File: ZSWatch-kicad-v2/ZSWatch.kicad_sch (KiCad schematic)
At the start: 71 parts, among them IC1 ESDALC6V1W5, IC2 XC9265C181MR-G, IC3 TPS61023DRLT, IC4 MAX30101EFD+T, IC5 FAN5622SX, IC6 BMI270, IC7 LIS2MDLTR, J2 Charger and programming heade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, M1 Vibrator DC Motor, U1 MAX1811ESA+, U10 0_NORA-B106, U11 NTS0104GU12, U13 GC9A01A_CST816S, U2 DMC2400UV-7, U3 NCV300LSN36T1G, U4 BMP581, U5 BME688, U6 DRV2603RUNT, U7 XC9265A331MR-G

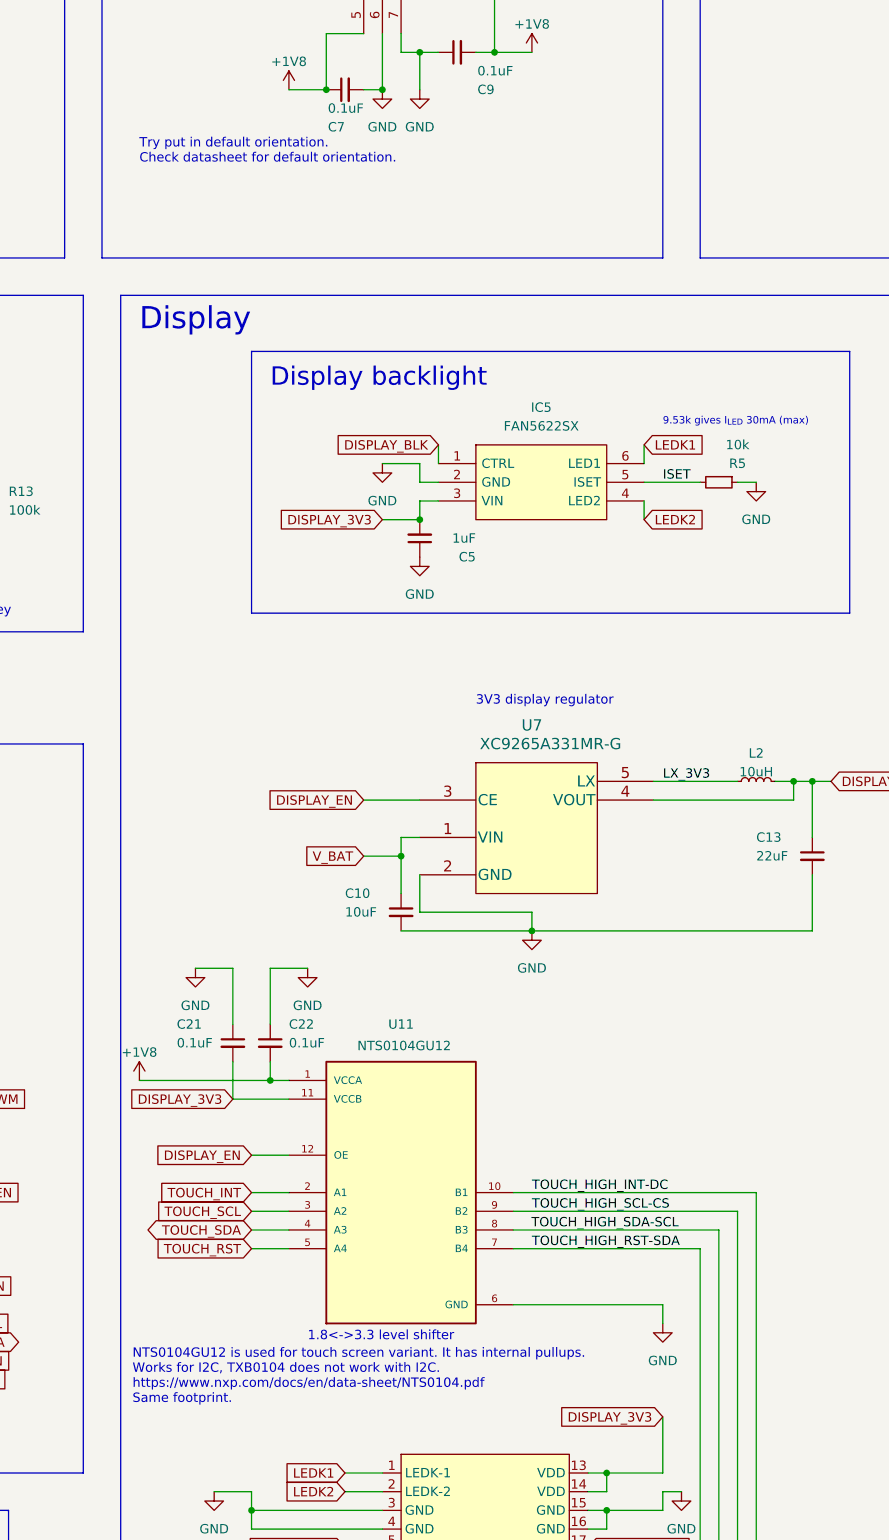
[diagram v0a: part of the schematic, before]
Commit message: Schematic: Re-generate latest schematic after some cleanup. Remove obsolete v1 kicad project.
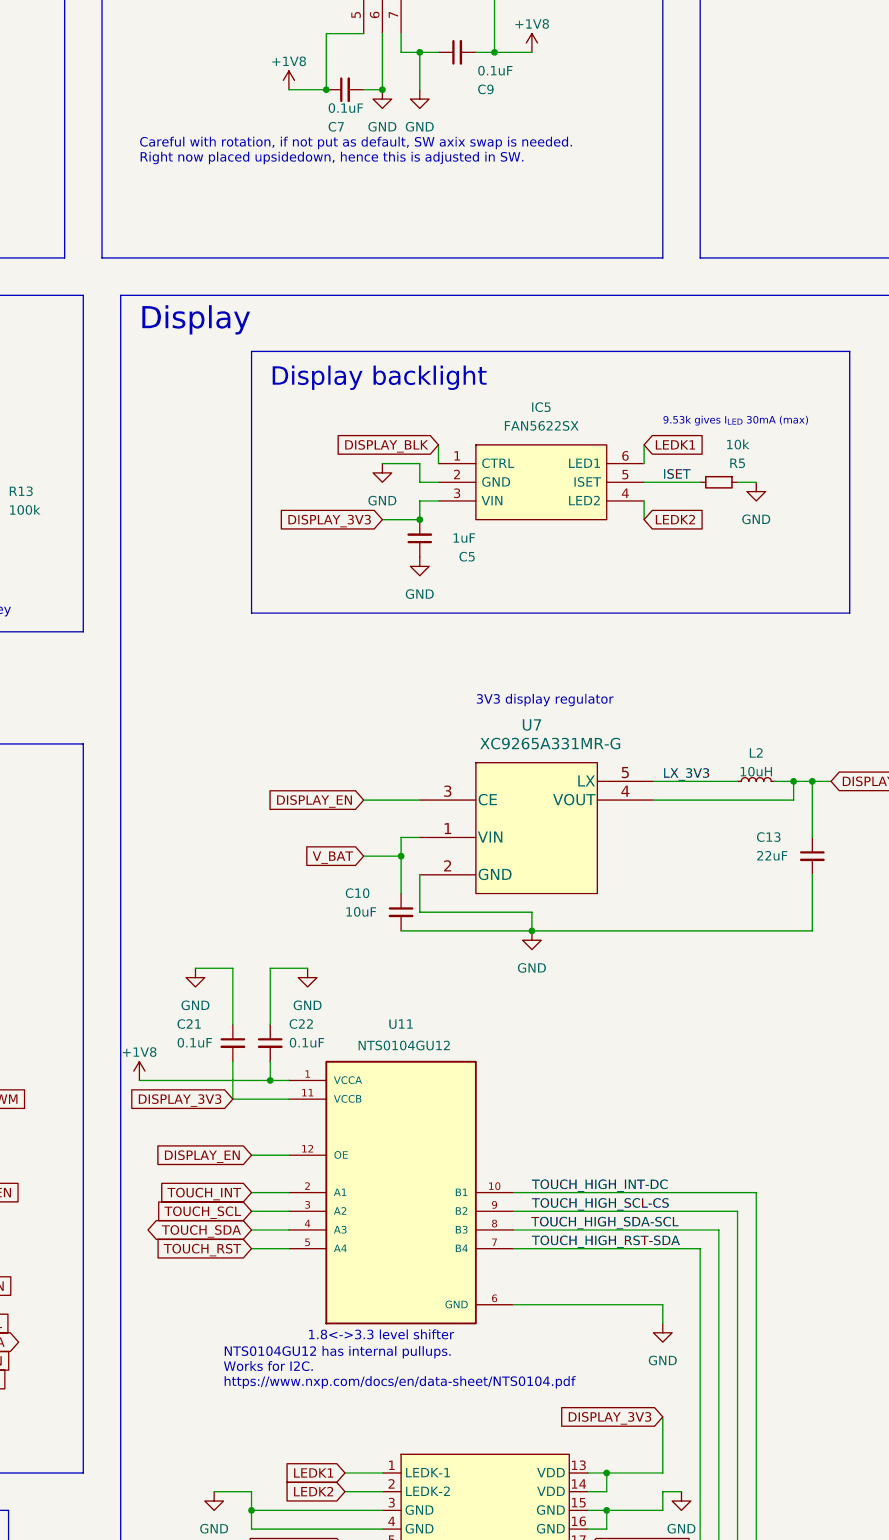
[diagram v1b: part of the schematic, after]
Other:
- note added: "Careful with rotation, if not put as default, SW axix swap is needed. Right now placed upsidedown, hence this is adjusted in SW."
- note added: "NTS0104GU12 has internal pullups. Works for I2C. https://www.nxp.com/docs/en/data-sheet/NTS0104.pdf"
- note removed: "NTS0104GU12 is used for touch screen variant. It has internal pullups. Works for I2C, TXB0104 does not work with I2C. https://www.nxp.com/docs/en/data-sheet/NTS0104.pdf Same footprint."
- note removed: "Try put in default orientation. Check datasheet for default orientation."
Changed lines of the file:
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@@
     (effects (font (size 1.27 1.27)) (justify left bottom))
   )
-  (text "NTS0104GU12 is used for touch screen variant. It has internal pullups.\nWorks for I2C, TXB0104 does not work with I2C.\nhttps://www.nxp.com/docs/en/data-sheet/NTS0104.pdf\nSame footprint."
-    (at 237.8198 275.2248 0)
+  (text "NTS0104GU12 has internal pullups.\nWorks for I2C.\nhttps://www.nxp.com/docs/en/data-sheet/NTS0104.pdf"
+    (at 250.19 273.05 0)
     (effects (font (size 1.27 1.27)) (justify left bottom))
   )
@@
     (effects (font (size 1.27 1.27)) (justify left bottom))
   )
-  (text "Try put in default orientation.\nCheck datasheet for default orientation."
+  (text "Careful with rotation, if not put as default, SW axix swap is needed.\nRight now placed upsidedown, hence this is adjusted in SW."
     (at 238.76 106.68 0)
     (effects (font (size 1.27 1.27)) (justify left bottom))

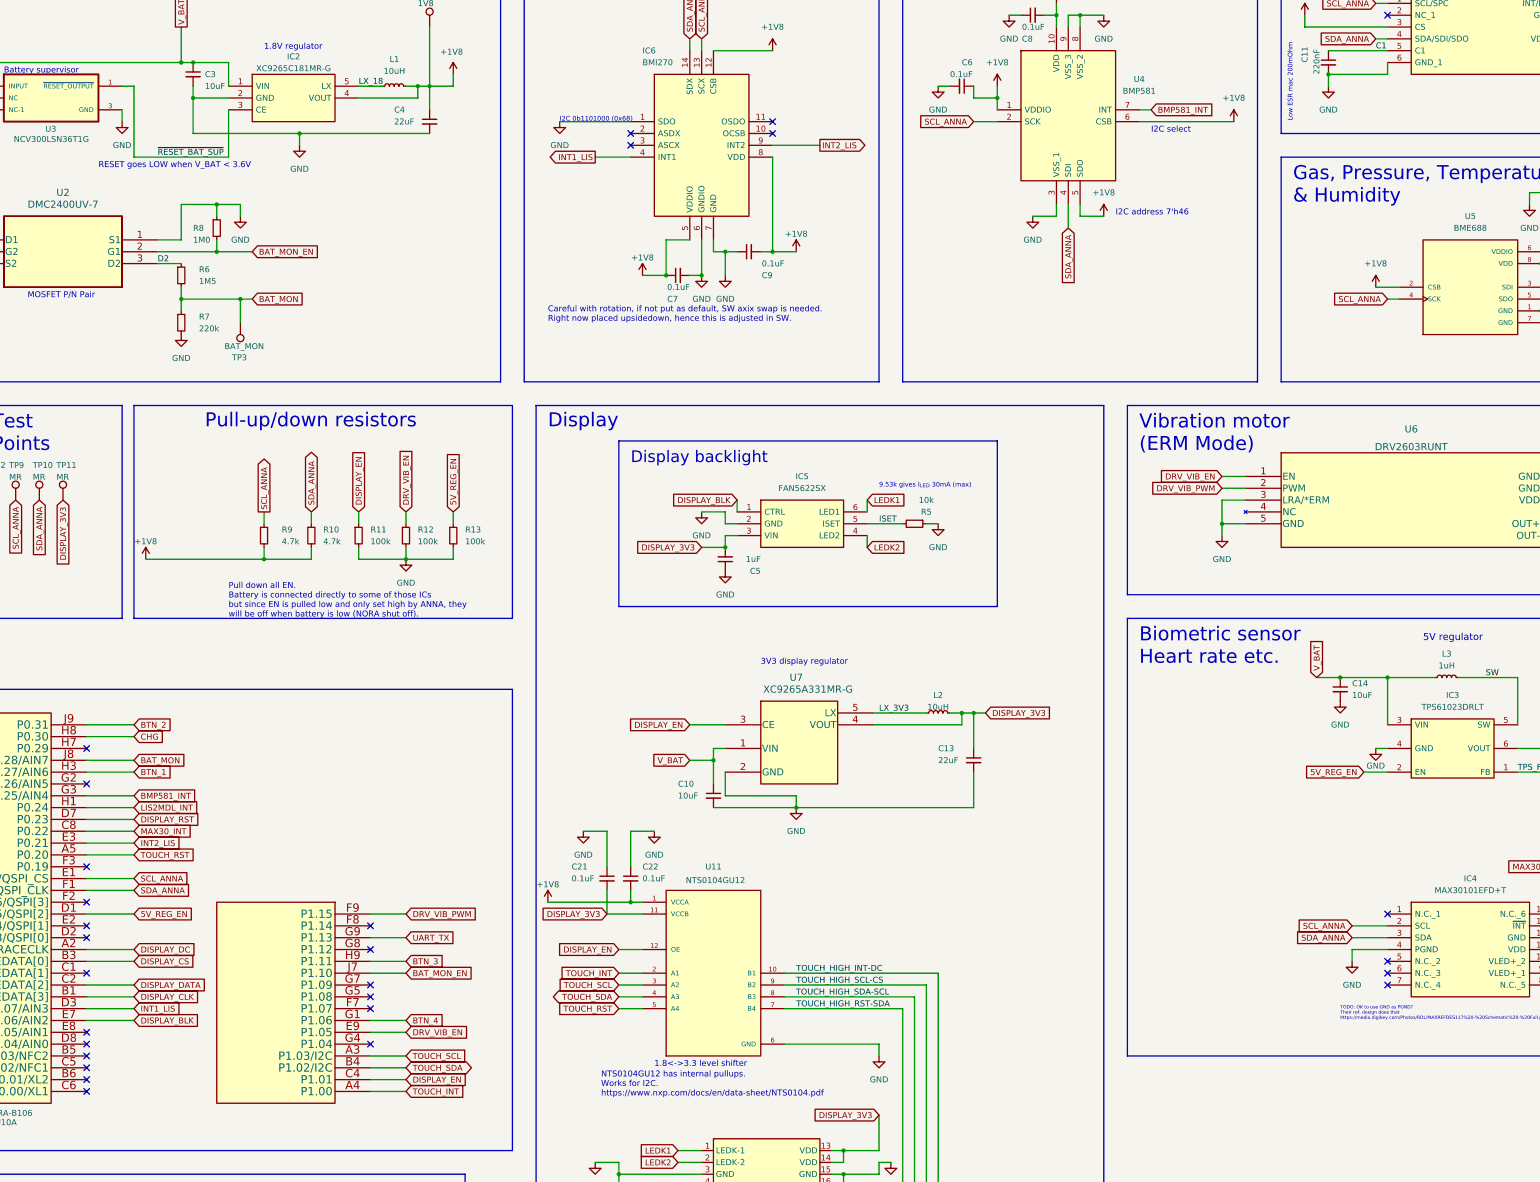
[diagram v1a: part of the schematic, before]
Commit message: Initial hardware changes to add an external flash (AT25SL128A) to ZSwatch.
Signed-off-by: Victor Chavez <vchavezb@protonmail.com>
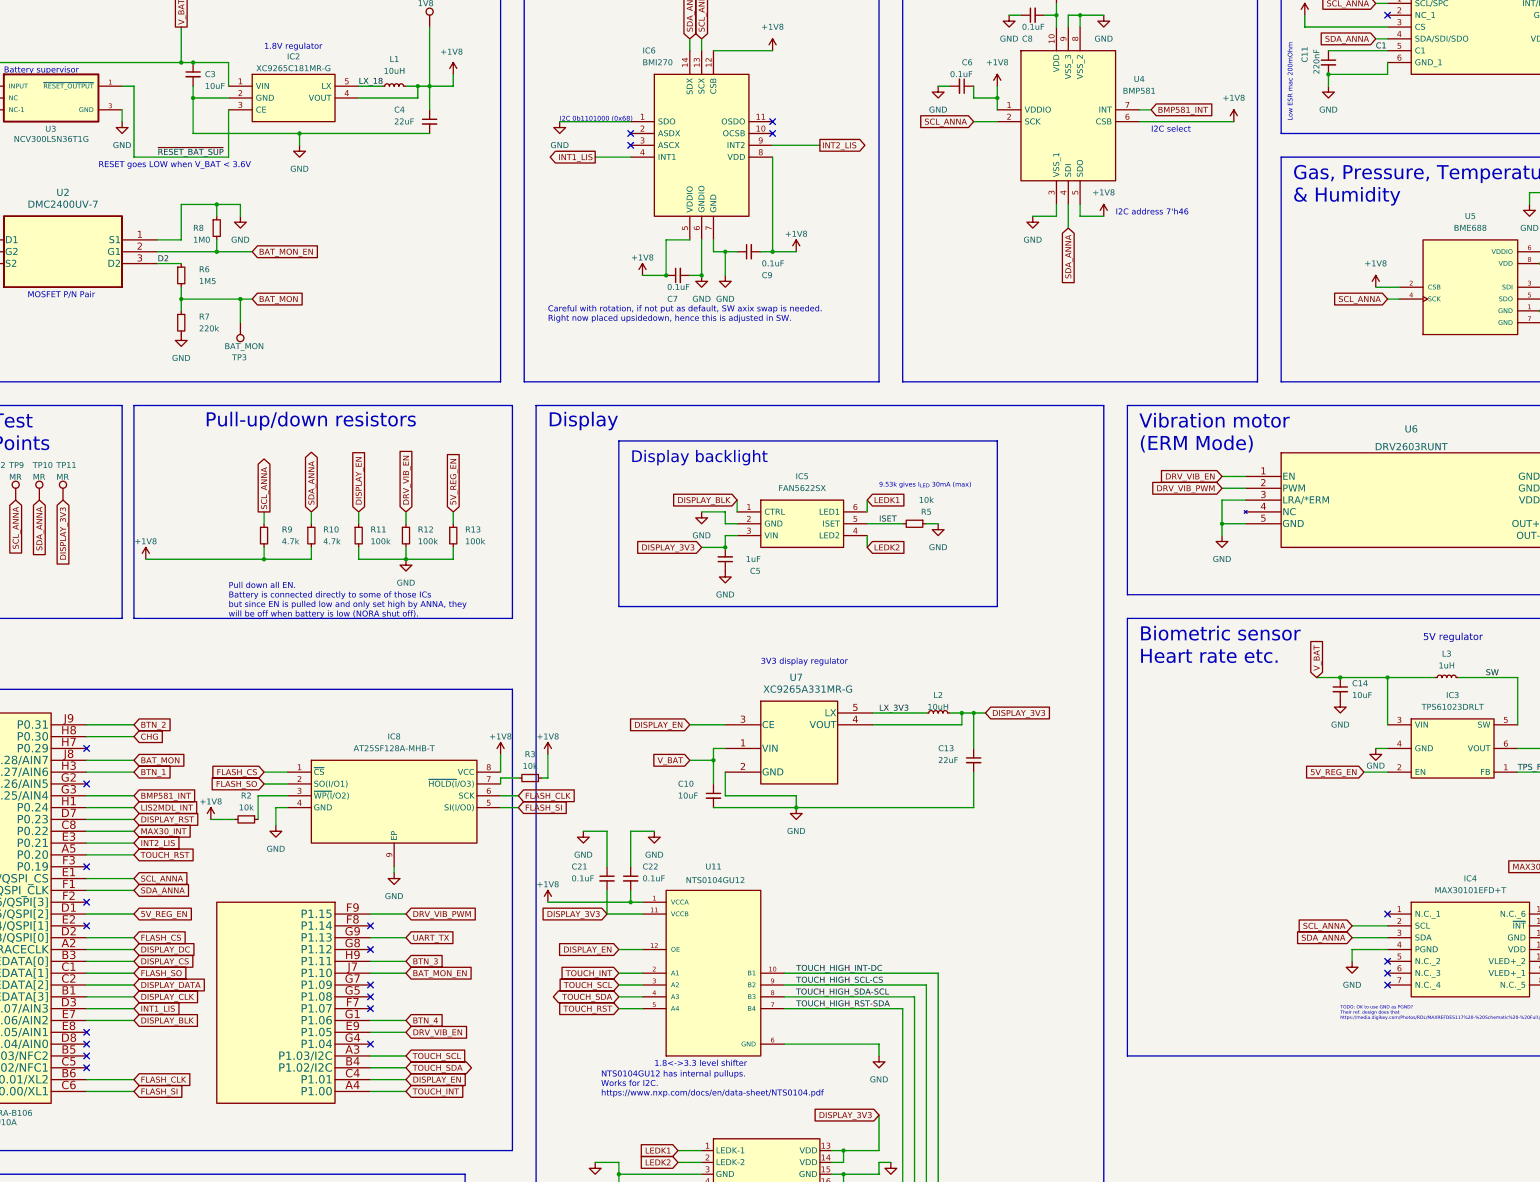
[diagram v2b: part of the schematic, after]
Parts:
- added IC8: AT25SF128A-MHB-T, flash:SON127P600X500X60-9N-D, symbol Flash:AT25SF128A-MHB-T
- added R2, R3: 10k, Resistor_SMD:R_0603_1608Metric, symbol Device:R_Small
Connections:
- net +1V8: now also IC8.8 (VCC), R2.2, R3.1
- net GND: now also IC8.4 (GND), IC8.9 (EP)
- net FLASH_CLK: now reaches U10.B6 (P0.01/XL2)
- net FLASH_CLK: now also IC8.6 (SCK)
- net FLASH_SO: now reaches U10.C1 (P0.10/TRACEDATA[1])
- net FLASH_SO: now also IC8.2 (SO(I/O1))
- net FLASH_SI: now reaches U10.C6 (P0.00/XL1)
- net FLASH_SI: now also IC8.5 (SI(I/O0))
- net FLASH_CS: now reaches U10.D2 (P0.13/QSPI[0])
- net FLASH_CS: now also IC8.1 (~{CS})
- new net: IC8.7 (~{HOLD(I}/O3)), R3.2
- new net: IC8.3 (~{WP(I}/O2)), R2.1
- no-connect marks 57 -> 53
